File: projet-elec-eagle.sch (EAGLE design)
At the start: 14 parts, among them IC1 PIC16F877P

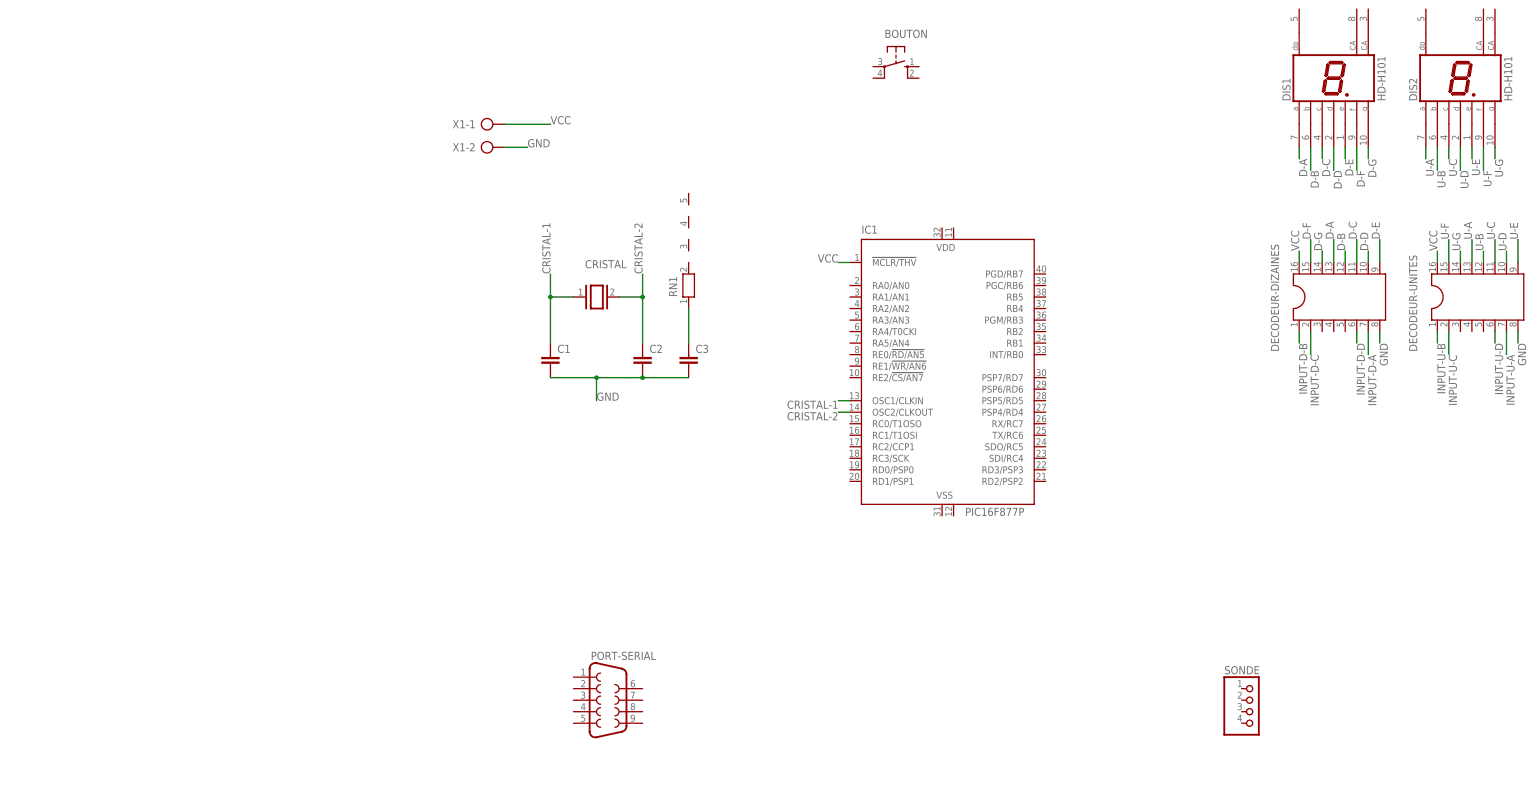
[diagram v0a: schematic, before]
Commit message: ajout port serial, sonde, ...
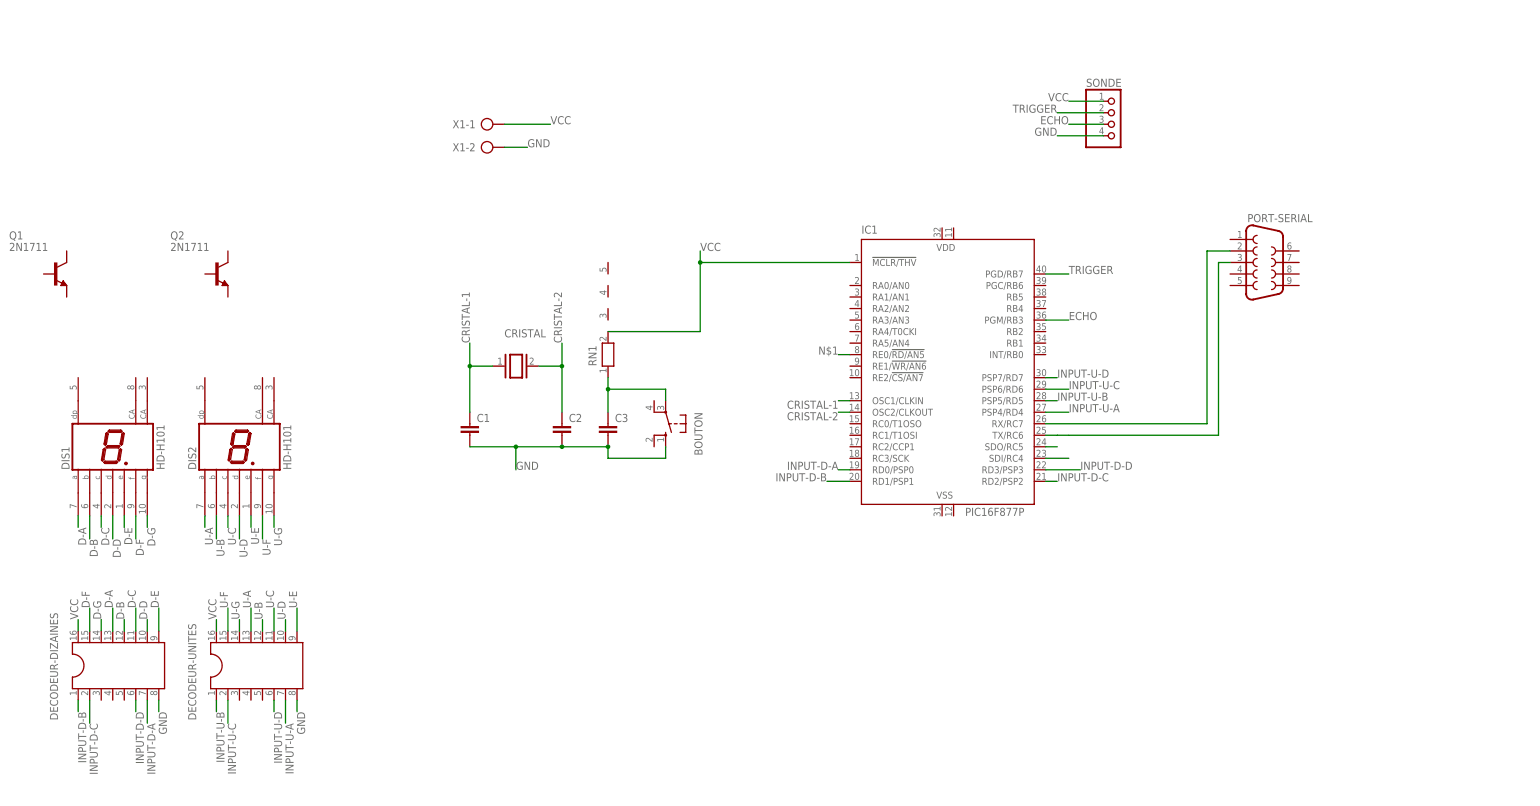
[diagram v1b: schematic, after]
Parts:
- added Q1, Q2: 2N1711, transistor-npn:2N1711
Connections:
- new net ECHO: IC1.PGM/RB3, SONDE.3
- new net N$1: IC1.RE0/!RD/AN5
- new net N$6: IC1.RX/RC7, PORT-SERIAL.2
- new net N$7: IC1.TX/RC6, PORT-SERIAL.3
- new net N$8: IC1.SDO/RC5
- new net N$9: IC1.SDI/RC4
- new net TRIGGER: IC1.PGD/RB7, SONDE.2
- net GND: now also BOUTON.S, SONDE.4
- net INPUT-D-A: now also IC1.RD0/PSP0
- net INPUT-D-B: now also IC1.RD1/PSP1
- net INPUT-D-C: now also IC1.RD2/PSP2
- net INPUT-D-D: now also IC1.RD3/PSP3
- net INPUT-U-A: now also IC1.PSP4/RD4
- net INPUT-U-B: now also IC1.PSP5/RD5
- net INPUT-U-C: now also IC1.PSP6/RD6
- net INPUT-U-D: now also IC1.PSP7/RD7
- net N$4: now also BOUTON.P
- net VCC: now also RN1.2, SONDE.1
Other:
- moved on the sheet: BOUTON, C1, C2, C3, CRISTAL, DECODEUR-DIZAINES, DECODEUR-UNITES, DIS1, DIS2, PORT-SERIAL, RN1, SONDE
